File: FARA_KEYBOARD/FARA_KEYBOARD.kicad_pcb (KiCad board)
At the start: 2 copper layers, 93.2 x 39.4 mm, 11 parts, among them J1 Conn_01x07_Pin, SW1 SW_Push, SW2 SW_Push, SW3 SW_Push, SW4 SW_Push, SW5 SW_Push, SW6 SW_Push

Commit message: v0.3 Circuit was completed
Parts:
- removed the REF** at (104.3, 53.0)
- removed the REF** at (104.3, 21.0)
- removed the REF** at (18.3, 53.0)
- removed the REF** at (18.3, 21.0)
- added J2: Conn_01x20, Connector_PinSocket_2.54mm:PinSocket_1x20_P2.54mm_Vertical, F.Cu at (54.3, 62.8)
- added J3: Conn_01x20, Connector_PinSocket_2.54mm:PinSocket_1x20_P2.54mm_Vertical, F.Cu at (54.3, 58.2)
- added J4: Conn_01x04, Connector_PinSocket_2.54mm:PinSocket_1x04_P2.54mm_Vertical, F.Cu at (64.0, 53.6)
- added J5: Conn_01x03, Connector_PinSocket_2.54mm:PinSocket_1x03_P2.54mm_Vertical, F.Cu at (54.3, 53.6)
- added J6: Conn_01x03, Connector_PinSocket_2.54mm:PinSocket_1x03_P2.54mm_Vertical, F.Cu at (54.3, 49.0)
- added J7: Conn_01x03, Connector_PinSocket_2.54mm:PinSocket_1x03_P2.54mm_Vertical, F.Cu at (54.3, 44.4)
- added J8: Conn_01x03, Connector_PinSocket_2.54mm:PinSocket_1x03_P2.54mm_Vertical, F.Cu at (54.3, 39.8)
- added J9: Conn_01x03, Connector_PinSocket_2.54mm:PinSocket_1x03_P2.54mm_Vertical, F.Cu at (54.3, 35.2)
- added R1: 4.7k, Resistor_SMD:R_0603_1608Metric_Pad0.98x0.95mm_HandSolder, F.Cu at (63.0, 49.1)
- added R2: 4.7k, Resistor_SMD:R_0603_1608Metric_Pad0.98x0.95mm_HandSolder, F.Cu at (65.5, 49.1)
- added R3: 0, Resistor_SMD:R_0201_0603Metric, F.Cu at (67.6, 50.1)
- added R4: 0, Resistor_SMD:R_0201_0603Metric, F.Cu at (69.4, 50.1)
- added REF**: MountingHole_3.2mm_M3, MountingHole:MountingHole_3.2mm_M3, F.Cu at (105.2, 94.0)
- added REF**: MountingHole_3.2mm_M3, MountingHole:MountingHole_3.2mm_M3, F.Cu at (105.2, 83.6)
- added REF**: MountingHole_3.2mm_M3, MountingHole:MountingHole_3.2mm_M3, F.Cu at (52.2, 94.0)
- added REF**: MountingHole_3.2mm_M3, MountingHole:MountingHole_3.2mm_M3, F.Cu at (52.2, 83.6)
- added REF**: MountingHole_3.2mm_M3, MountingHole:MountingHole_3.2mm_M3, F.Cu at (78.7, 94.0)
- SW1, SW2, SW3, SW4, SW5, SW6: footprint Button_Switch_THT:SW_PUSH-12mm -> Button_Switch_THT:SW_PUSH_6mm
- moved J1 75.2 mm to (57.6, 94.4)
- moved SW1 51.5 mm to (57.5, 88.9)
- moved SW2 48.7 mm to (65.1, 88.9)
- moved SW3 46.3 mm to (72.7, 88.9)
- moved SW4 44.4 mm to (80.3, 88.9)
- moved SW5 43.0 mm to (87.9, 88.9)
- moved SW6 42.1 mm to (95.5, 88.9)
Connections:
- net Net-(J1-Pin_1) renamed SW1
- net Net-(J1-Pin_2) renamed SW2
- net Net-(J1-Pin_3) renamed SW3
- net Net-(J1-Pin_4) renamed SW4
- net Net-(J1-Pin_5) renamed SW5
- net Net-(J1-Pin_6) renamed SW6
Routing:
- net SW6: track 69.8 -> 35.8 mm
- net SW5: track 60.6 -> 28.9 mm
- net SW4: track 50.5 -> 24.6 mm
- net SW3: track 40.6 -> 19.0 mm
- net SW2: track 31.4 -> 14.1 mm
- net SW1: track 21.5 -> 12.7 mm
- net GND: vias 27 -> 16
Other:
- board size 93.2 x 39.4 mm -> 60 x 17.4 mm

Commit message: v0.4 circuit is ready
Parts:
- added BZ1: Buzzer, Connector_PinHeader_2.54mm:PinHeader_1x02_P2.54mm_Vertical, F.Cu at (143.5, 68.9)
- added J10: Conn_01x02, Connector_PinSocket_2.54mm:PinSocket_1x02_P2.54mm_Vertical, F.Cu at (138.6, 61.8)
- added J11: Screw_Terminal_01x02, Connector_PinSocket_2.54mm:PinSocket_1x02_P2.54mm_Vertical, F.Cu at (143.2, 61.8)
- added J12: Screw_Terminal_01x02, Connector_PinSocket_2.54mm:PinSocket_1x02_P2.54mm_Vertical, F.Cu at (147.8, 61.8)
- added J13: Conn_01x02, Connector_PinSocket_2.54mm:PinSocket_1x02_P2.54mm_Vertical, F.Cu at (152.4, 61.8)
- added Q1: AO3400A, Package_TO_SOT_SMD:SOT-23, F.Cu at (138.7, 68.8)
- added Q2: AO3400A, Package_TO_SOT_SMD:SOT-23, F.Cu at (138.7, 73.2)
- added R5: 0, Resistor_SMD:R_0201_0603Metric, F.Cu at (147.1, 67.5)
- added R6: 0, Resistor_SMD:R_0201_0603Metric, F.Cu at (147.1, 69.2)
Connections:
- J2 pad 14: Net-(J2-Pin_14) -> buzzer
- J2 pad 20: Net-(J2-Pin_20) -> lasers
- J3 pad 16: STRIP1 -> STRIP0
- J3 pad 17: STRIP2 -> STRIP1
- J3 pad 19: STRIP3 -> STRIP2
- J3 pad 20: STRIP4 -> STRIP3
- J3 pad 5: Net-(J3-Pin_5) -> LEDS
- J6 pad 2: STRIP1 -> STRIP0
- J7 pad 2: STRIP2 -> STRIP1
- J8 pad 2: STRIP3 -> STRIP2
- J9 pad 2: STRIP4 -> STRIP3

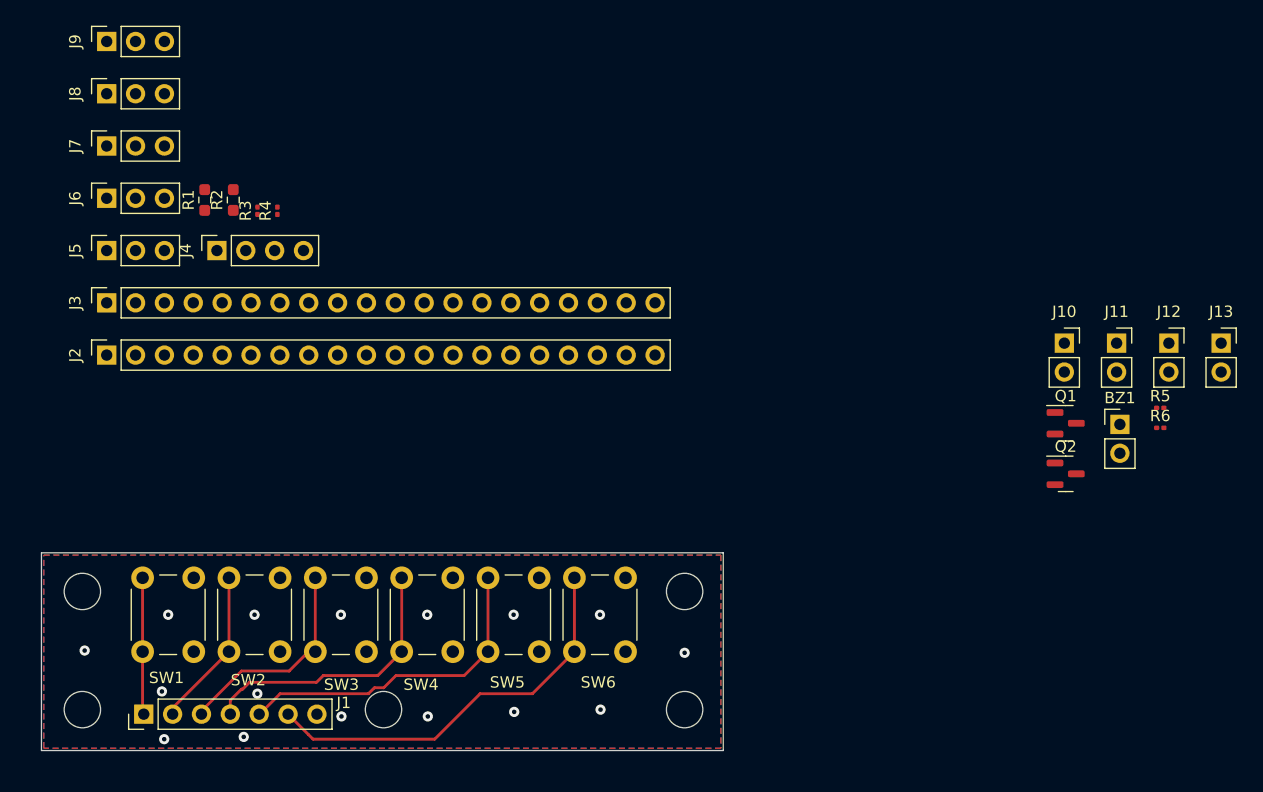
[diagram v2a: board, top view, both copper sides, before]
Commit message: v0.5 draft PCB was routed
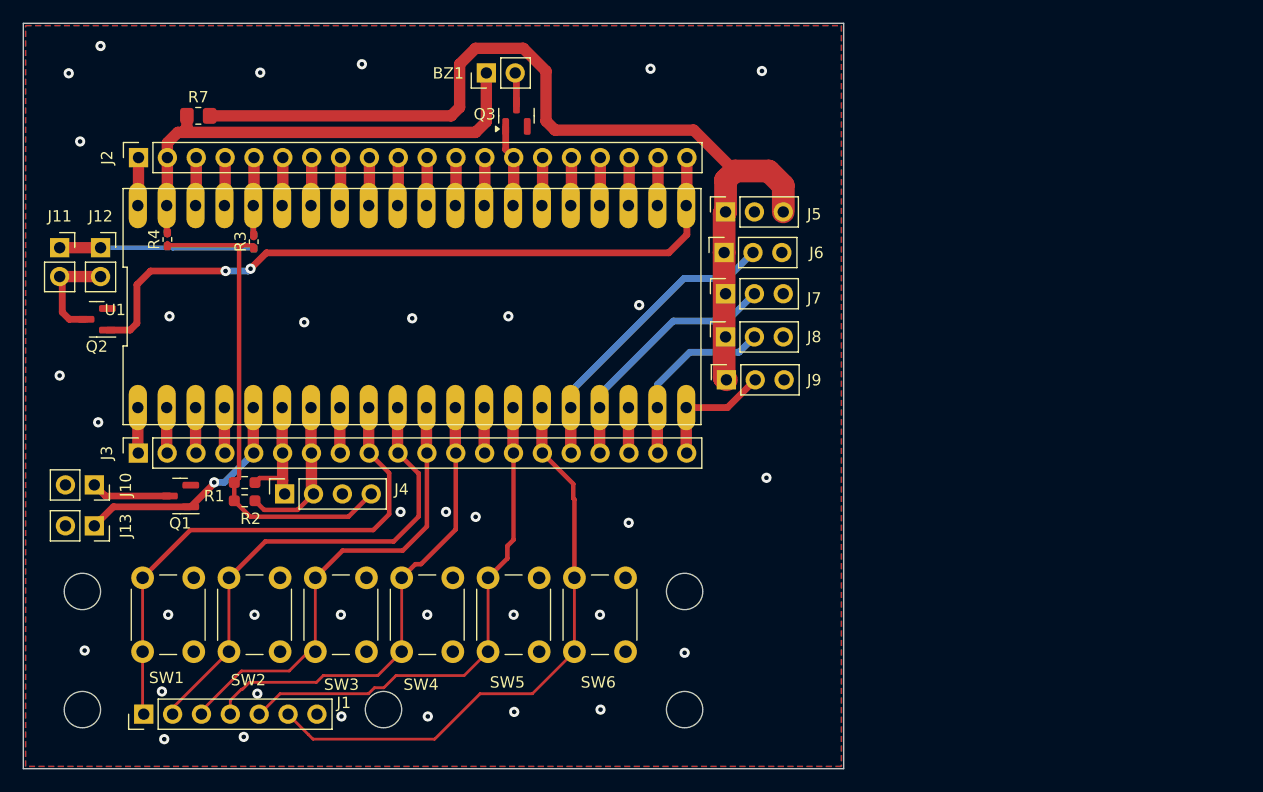
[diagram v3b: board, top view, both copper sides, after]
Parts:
- added Q3: AO3400A, Package_TO_SOT_SMD:SOT-23, F.Cu at (90.4, 41.7)
- added R7: 0, Resistor_SMD:R_0805_2012Metric_Pad1.20x1.40mm_HandSolder, F.Cu at (62.4, 41.7)
- added U1: Raspberri_Pi_Pico, myLib8:Raspberry Pi Pico, F.Cu at (81.2, 58.5)
- R3, R4: footprint Resistor_SMD:R_0201_0603Metric -> Resistor_SMD:R_0402_1005Metric_Pad0.72x0.64mm_HandSolder
- R5, R6: footprint Resistor_SMD:R_0201_0603Metric -> Resistor_SMD:R_0402_1005Metric_Pad0.72x0.64mm_HandSolder; moved to B.Cu
- moved J13 100.5 mm to (53.2, 77.8), turned to -90 degrees
- moved J12 94.4 mm to (53.8, 53.4)
- moved J11 93.4 mm to (50.2, 53.4)
- moved R5 88.6 mm to (59.7, 52.6), turned to 90 degrees
- moved Q2 86.4 mm to (53.5, 59.6), turned to 180 degrees
- moved J10 86.3 mm to (53.2, 74.2), turned to -90 degrees
- moved R6 81.4 mm to (67.3, 52.8), turned to 90 degrees
- moved Q1 78.2 mm to (60.8, 75.2), turned to 180 degrees
- moved BZ1 63.8 mm to (87.8, 38.0), turned to 90 degrees
- moved J9 62.1 mm to (108.9, 65.0)
- moved J8 58.5 mm to (108.8, 61.2)
- moved J7 56.0 mm to (108.8, 57.4)
- moved J5 54.6 mm to (108.8, 50.2)
- moved J6 54.5 mm to (108.7, 53.8)
- moved R2 26.5 mm to (66.5, 75.6), turned to 0 degrees
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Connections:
- BZ1 pad 1: buzzer -> +5V
- BZ1 pad 2: GND -> Net-(BZ1-+)
- J4 pad 4: Net-(J4-Pin_4) -> V_I2C
- R1 pad 1: +3V3 -> V_I2C
- R2 pad 1: +3V3 -> V_I2C
- R3 pad 1: Net-(J4-Pin_4) -> V_I2C
- R4 pad 1: Net-(J4-Pin_4) -> V_I2C
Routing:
- net VPP: track 0.00 -> 83.9 mm
- net lasers: track 0.00 -> 63.3 mm, vias 0 -> 2
- net +5V: track 0.00 -> 45.0 mm
- net V_I2C: track 0.00 -> 43.9 mm
- net SW1: track 12.7 -> 46.8 mm
- net GND: track 0.00 -> 33.0 mm, vias 16 -> 35
- net SW2: track 14.1 -> 43.4 mm
- net STRIP0: track 0.00 -> 26.5 mm
- net STRIP1: track 0.00 -> 22.5 mm
- net SW3: track 19.0 -> 41.1 mm
- net LEDS: track 0.00 -> 20.8 mm, vias 0 -> 1
- net V_lasers: track 0.00 -> 17.3 mm
- net SW4: track 24.6 -> 41.8 mm
- net STRIP2: track 0.00 -> 16.3 mm
- net SW6: track 35.8 -> 52.0 mm
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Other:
- board size 60 x 17.4 mm -> 72.2 x 65.6 mm

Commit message: v0.6 seems 2B ready
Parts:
- added D1: PMEG3010CEH, Diode_SMD:D_SOD-123F, B.Cu at (89.4, 140.6)
- added REF**: MountingHole_3.2mm_M3, MountingHole:MountingHole_3.2mm_M3, F.Cu at (52.2, 139.0)
- added REF**: MountingHole_3.2mm_M3, MountingHole:MountingHole_3.2mm_M3, F.Cu at (105.2, 139.0)
- BZ1, J10, J11, J12, J13, J2, J3, J4, J5, J6, J7, J8, J9, Q1, Q2, Q3, R1, R2, R3, R4, R7, U1: moved to B.Cu
- R5, R6: moved to F.Cu
- moved BZ1 99.7 mm to (88.0, 137.7), turned to -90 degrees
- moved R7 92.9 mm to (62.6, 134.6)
- moved Q3 92.1 mm to (90.6, 133.9), turned to -90 degrees
- moved J2 84.8 mm to (57.3, 130.2), turned to -90 degrees
- moved J5 75.2 mm to (109.0, 125.4), turned to -90 degrees
- moved R4 70.4 mm to (59.9, 123.0), turned to -90 degrees
- moved R5 70.4 mm to (59.9, 123.0), turned to -90 degrees
- moved R3 70.0 mm to (67.5, 122.8), turned to -90 degrees
- moved R6 70.0 mm to (67.5, 122.8), turned to -90 degrees
- moved J11 68.9 mm to (50.4, 122.3)
- moved J12 68.9 mm to (54.0, 122.3)
- moved J6 68.1 mm to (108.9, 121.8), turned to -90 degrees
- moved J7 60.8 mm to (109.0, 118.2), turned to -90 degrees
- moved U1 58.6 mm to (81.4, 117.1)
- moved Q2 56.3 mm to (53.7, 116.0)
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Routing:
- net SW5: track 44.8 -> 62.3 mm
- net SW4: track 41.8 -> 56.2 mm
- net SW3: track 41.1 -> 51.0 mm
- net Net-(BZ1-+): track 2.88 -> 5.97 mm
- net SW2: track 43.4 -> 46.4 mm
- net +5V: track 45.0 -> 47.7 mm
- net VPP: track 83.9 -> 86.0 mm
- net Net-(J10-Pin_1): track 7.02 -> 8.68 mm
- net SW6: track 52.0 -> 53.6 mm
- net STRIP0: track 26.5 -> 27.9 mm
- net LEDS: track 20.8 -> 21.7 mm
- net STRIP1: track 22.5 -> 23.3 mm
- net GND: vias 35 -> 148
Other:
- board size 72.2 x 65.6 mm -> 71 x 63.8 mm

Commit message: v0.7 form was corrected
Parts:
- removed the REF** at (52.2, 139.0)
- removed the REF** at (105.2, 139.0)
- added J14: Conn_01x02, Connector_PinSocket_2.54mm:PinSocket_1x02_P2.54mm_Vertical, F.Cu at (111.5, 132.6)
- moved D1 40.6 mm to (51.8, 125.4)
- moved Q3 38.2 mm to (52.4, 132.0), turned to 0 degrees
- moved BZ1 38.2 mm to (50.9, 128.4)
- moved R7 5.39 mm to (57.4, 133.2), turned to 180 degrees
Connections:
- net Net-(J2-Pin_17) renamed FLT_I/O
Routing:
- net buzzer: track 7.28 -> 47.4 mm, vias 0 -> 1
- net FLT_I/O: track 4.24 -> 22.4 mm
- net +5V: track 47.7 -> 32.0 mm
- net VPP: track 86.0 -> 82.8 mm
- net Net-(BZ1-+): track 5.97 -> 6.87 mm
- net GND: vias 148 -> 161
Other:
- board size 71 x 63.8 mm -> 69.1 x 56 mm

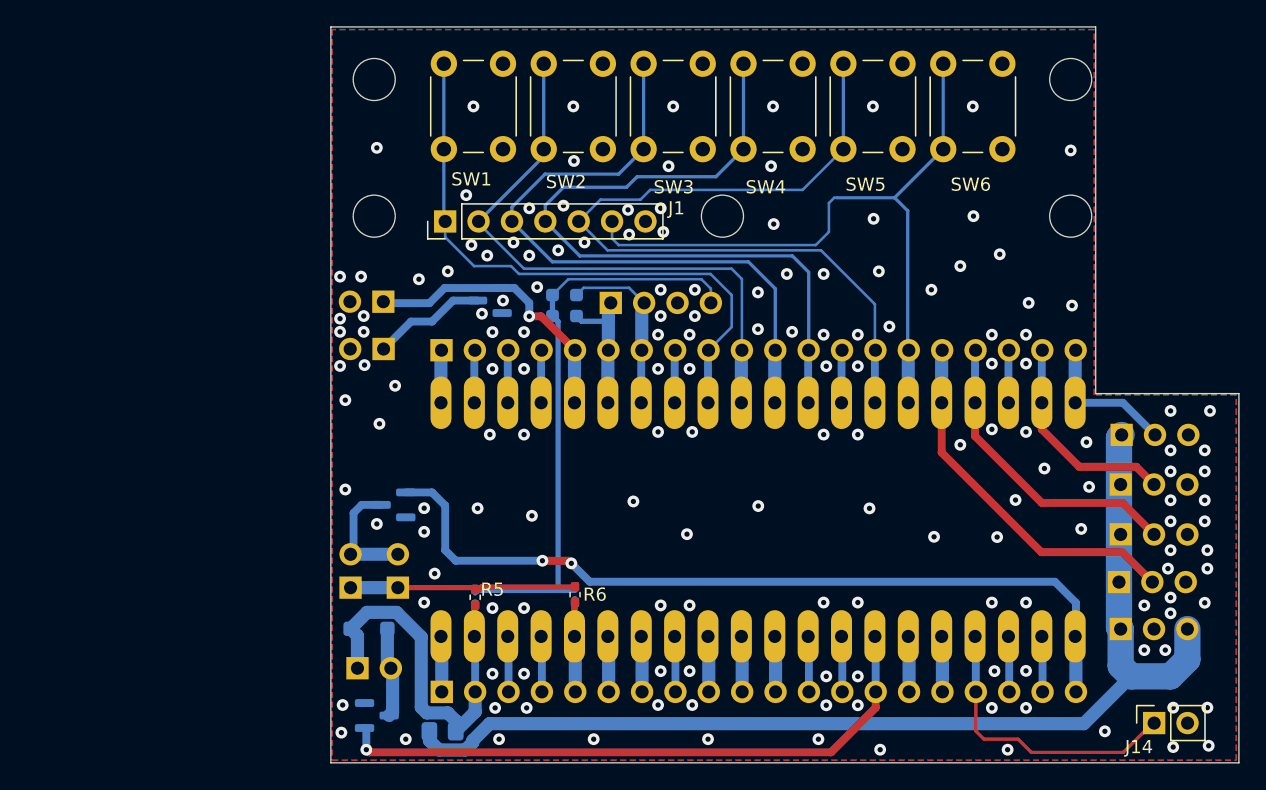
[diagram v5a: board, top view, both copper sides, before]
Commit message: v0.8 reverted, ordered advanced.
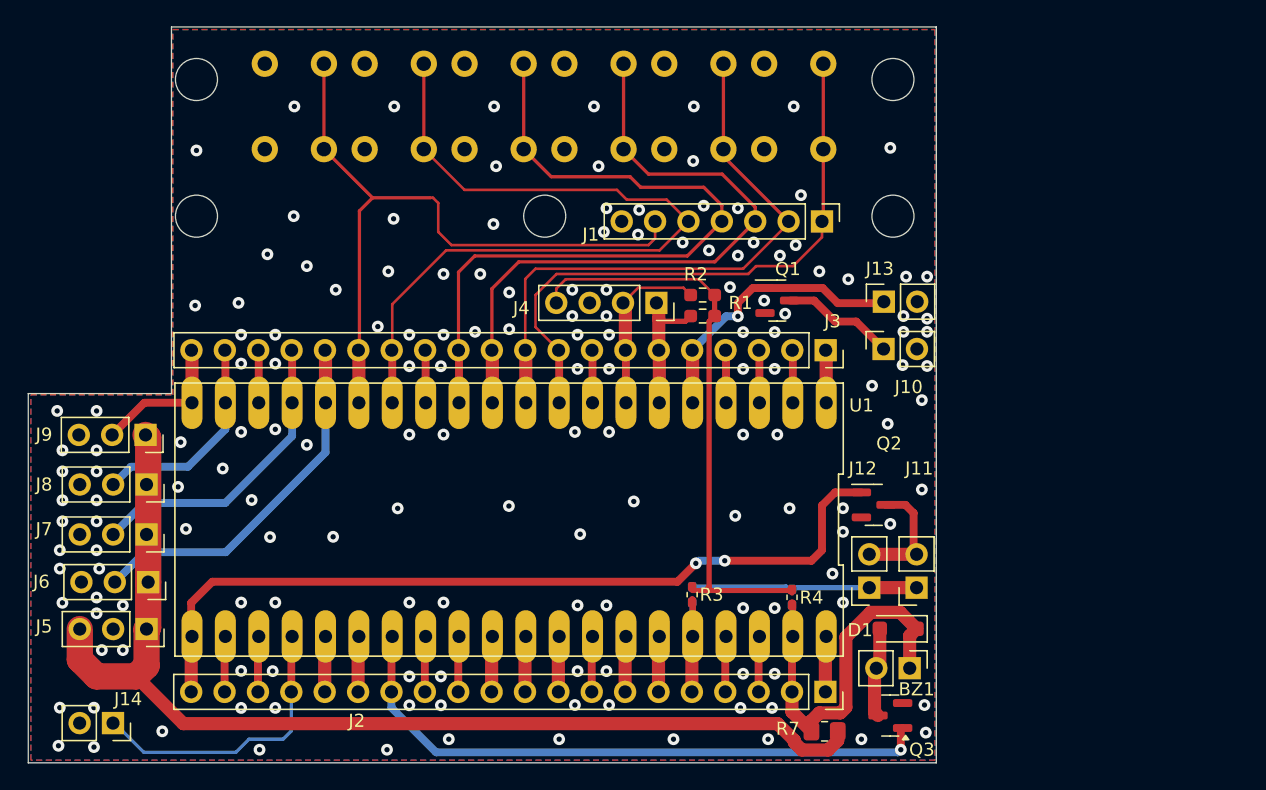
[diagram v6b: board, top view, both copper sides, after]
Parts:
- BZ1, D1, J10, J11, J12, J13, J2, J3, J4, J5, J6, J7, J8, J9, Q1, Q2, Q3, R1, R2, R3, R4, R7, U1: moved to F.Cu
- R5, R6, REF** (x5), SW1, SW2, SW3, SW4, SW5, SW6: moved to B.Cu
- moved J14 79.2 mm to (32.3, 132.6), turned to -90 degrees
- moved J9 74.3 mm to (34.8, 110.6)
- moved J5 74.1 mm to (34.9, 125.4)
- moved J7 74.1 mm to (34.9, 118.2)
- moved J8 74.1 mm to (34.9, 114.4)
- moved J6 73.9 mm to (35.0, 121.8)
- moved REF** 66.5 mm to (38.7, 94.0), turned to 180 degrees
- moved REF** 66.5 mm to (38.7, 83.6), turned to 180 degrees
- moved SW6 47.1 mm to (48.4, 88.9)
- moved J11 43.1 mm to (93.5, 122.3), turned to 180 degrees
- moved BZ1 42.0 mm to (92.9, 128.4)
- moved D1 40.3 mm to (92.1, 125.4), turned to 180 degrees
- moved REF** 39.5 mm to (91.7, 94.0), turned to 180 degrees
- moved REF** 39.5 mm to (91.7, 83.6), turned to 180 degrees
- moved Q3 39.1 mm to (91.5, 132.0), turned to 180 degrees
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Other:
- outline, holes or cut-outs redrawn
